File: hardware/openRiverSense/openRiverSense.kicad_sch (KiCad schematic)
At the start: 42 parts, among them J1 Conn_02x04_Odd_Even, J2 Conn_01x08_Pin, J3 Conn_01x02_Pin, U1 MCP6002T-I_SN, U2 MCP6002T-I_SN, U3 MCP6002T-I_SN, U4 AO3401A, U5 MCP6002T-I_SN

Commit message: PCB Design Move to UF2 bootloader Move to Adafruit TinyUSB for mass storage Update Formatting Flip UI orientation Change to PWM Backlight
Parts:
- removed C11, C2, C7, C8: 0402,100nF,16V,X7R, C_0402_1005Metric, symbol jlcpcb-basic-capacitor:0402,100nF,16V,X7R
- removed C5: 0402,10uF,6.3V,X5R, C_0402_1005Metric, symbol jlcpcb-basic-capacitor:0402,10uF,6.3V,X5R
- removed D1: ZMM3V3, footprint:LL-34_L3.5-W1.5-RD, symbol jlcpcb-diodes:ZMM3V3
- removed J1: Conn_02x04_Odd_Even, Connector_PinHeader_2.00mm:PinHeader_2x04_P2.00mm_Horizontal, symbol Connector_Generic:Conn_02x04_Odd_Even
- removed J2: Conn_01x08_Pin, Connector_PinHeader_2.54mm:PinHeader_1x08_P2.54mm_Vertical, symbol Connector:Conn_01x08_Pin
- removed J3: Conn_01x02_Pin, Connector_Wire:SolderWire-0.1sqmm_1x02_P3.6mm_D0.4mm_OD1mm, symbol Connector:Conn_01x02_Pin
- removed JP1: SolderJumper_2_Bridged, Jumper:SolderJumper-2_P1.3mm_Bridged_Pad1.0x1.5mm, symbol Jumper:SolderJumper_2_Bridged
- removed L1, L2, L3: GZ1608D601TF, Inductor_SMD:L_0603_1608Metric, symbol jlcpcb-inductors-ferrite-beads:GZ1608D601TF
- removed LED1: Green, LED_SMD:LED_0603_1608Metric, symbol jlcpcb-diodes:19-217_GHC-YR1S2_3T
- removed R1, R3: 0603,22k, R_0603_1608Metric, symbol jlcpcb-basic-resistor:0603,22k
- removed R10: 0805,16k, R_0805_2012Metric, symbol jlcpcb-basic-resistor:0805,16k
- removed R11, R12: 0402,10k, R_0402_1005Metric, symbol jlcpcb-basic-resistor:0402,10k
- removed R13: 0402,100k, R_0402_1005Metric, symbol jlcpcb-basic-resistor:0402,100k
- removed R15, R7: 0603,20k, R_0603_1608Metric, symbol jlcpcb-basic-resistor:0603,20k
- removed R16, R2, R5: 0603,10k, R_0603_1608Metric, symbol jlcpcb-basic-resistor:0603,10k
- removed R17, R9: 0603,5.1k, R_0603_1608Metric, symbol jlcpcb-basic-resistor:0603,5.1k
- removed R4: 0603,18k, R_0603_1608Metric, symbol jlcpcb-basic-resistor:0603,18k
- removed R6: 0603,11k, R_0603_1608Metric, symbol jlcpcb-basic-resistor:0603,11k
- removed R8: 0603,51k, R_0603_1608Metric, symbol jlcpcb-basic-resistor:0603,51k
- removed U1, U2, U3, U5: MCP6002T-I_SN, footprint:SOIC-8_L4.9-W3.9-P1.27-LS6.0-BL, symbol jlcpcb-analog:MCP6002T-I_SN
- added B1: CR1220, footprint:BAT-SMD_BS-12-B2AA002, symbol jlcpcb-extended:CR1220
- added BMS1: Li-ion 500mA TP4057, footprint:SOT-23-6_L2.9-W1.6-P0.95-LS2.8-BL, symbol jlcpcb-power:Li-ion 500mA TP4057
- added BMS2: SLM6500, footprint:SOP-8_L4.9-W3.9-P1.27-LS6.0-BL-EP, symbol jlcpcb-extended:SLM6500
- added C11, C13, C2, C7: 10uF, footprint:0402_1005Metric, symbol jlcpcb-basic-capacitor:0402,10uF,6.3V,X5R
- added C12, C15: 100nF, footprint:0402_1005Metric, symbol jlcpcb-basic-capacitor:0402,100nF,16V,X7R
- added C14: 0402,1uF,25V,X5R, footprint:0402_1005Metric, symbol jlcpcb-basic-capacitor:0402,1uF,25V,X5R
- added C16: 10uF,6.3V, footprint:0402_1005Metric, symbol jlcpcb-basic-capacitor:0402,10uF,6.3V,X5R
- added C17: 0603,22uF,6.3V,X5R, footprint:0603_1608Metric, symbol jlcpcb-basic-capacitor:0603,22uF,6.3V,X5R
- added C5: 0603,10uF,10V,X5R, footprint:0603_1608Metric, symbol jlcpcb-basic-capacitor:0603,10uF,10V,X5R
- added C8: 0402,10uF,6.3V,X5R, footprint:0402_1005Metric, symbol jlcpcb-basic-capacitor:0402,10uF,6.3V,X5R
- added D1, D2, D3, D5, D6: 1N4148WS_T4, footprint:SOD-323_L1.8-W1.3-LS2.5-RD, symbol jlcpcb-diodes:1N4148WS_T4
- added D4: P6SMB6_8CA-C78395, footprint:SMB_L4.6-W3.6-LS5.3-BI, symbol jlcpcb-diodes:P6SMB6_8CA-C78395
- added ESD1: SRV05, footprint:SOT-23-6_L2.9-W1.6-P0.95-LS2.8-BR, symbol jlcpcb-diodes:SRV05
- added K1: ~, Kea Progmon:mpcie-full-card, symbol Kea Progmon:Kea_Progmon
- added L1: 3.3uH,6A, footprint:IND-SMD_L7.3-W6.8, symbol jlcpcb-extended:3.3uH,6A
- added LDO1, LDO2: XC6220B331MR-G, footprint:SOT-25_L3.0-W1.6-P0.95-LS2.8-TL, symbol jlcpcb-extended:XC6220B331MR-G
- added LED1, LED2, LED5, LED9: 0603,Green, footprint:LED0603, symbol jlcpcb-diodes:0603,Green
- added LED3, LED4, LED6, LED7, LED8: 0603,Yellow, footprint:LED0603, symbol jlcpcb-diodes:0603,Yellow
- added P1: USB-C, footprint:USB-C-SMD_G-SWITCH_GT-USB-7010ASV, symbol jlcpcb-extended:USB C
- added P2, P3: JSTSH_01x06_Vertical, footprint:CONN-SMD_6P-P1.00_DEALON_1.0-6PS, symbol jlcpcb-extended:JSTSH_01x06_Vertical
- added R1, R18, R34, R35: 100k, footprint:0402_1005Metric, symbol jlcpcb-basic-resistor:0402,100k
- added R10, R13, R27, R28, R30, R38, R41, R5, R7, R9: 0402,5.1k, footprint:0402_1005Metric, symbol jlcpcb-basic-resistor:0402,5.1k
- added R11, R21, R29, R36, R8: 0402,100k, footprint:0402_1005Metric, symbol jlcpcb-basic-resistor:0402,100k
- added R15, R16, R22, R6: 0402,10k, footprint:0402_1005Metric, symbol jlcpcb-basic-resistor:0402,10k
- added R19, R25: 0402,330, footprint:0402_1005Metric, symbol jlcpcb-basic-resistor:0402,330
- added R2, R26, R33: 47k, footprint:0402_1005Metric, symbol jlcpcb-basic-resistor:0402,47k
- added R20, R23, R24: 0402,47k, footprint:0402_1005Metric, symbol jlcpcb-basic-resistor:0402,47k
- added R3: 0603,330, footprint:0603_1608Metric, symbol jlcpcb-basic-resistor:0603,330
- added R31, R39: 100m, footprint:1206_3216Metric, symbol jlcpcb-basic-resistor:1206,100m
- added R32, R37: 0402,0,1A, footprint:0402_1005Metric, symbol jlcpcb-basic-resistor:0402,0,1A
- added R4: 0603,100k, footprint:0603_1608Metric, symbol jlcpcb-basic-resistor:0603,100k
- added R40: 0402,150k, footprint:0402_1005Metric, symbol jlcpcb-basic-resistor:0402,150k
- added R42: 0402,33k, footprint:0402_1005Metric, symbol jlcpcb-basic-resistor:0402,33k
- added SW1: Reset, footprint:SW-SMD_4P-L5.1-W5.1-P3.70-LS6.5-TL-2, symbol jlcpcb-switches:TS-1187A-B-A-B
- added SW2: UP_Button, footprint:SW-TH_4P-L12.0-W12.0-P5.00-LS12.5-EH, symbol jlcpcb-extended:Push_Button_SKHCBGA010
- added SW3: ENTER_Button, footprint:SW-TH_4P-L12.0-W12.0-P5.00-LS12.5-EH, symbol jlcpcb-extended:Push_Button_SKHCBGA010
- added SW4: DOWN_Button, footprint:SW-TH_4P-L12.0-W12.0-P5.00-LS12.5-EH, symbol jlcpcb-extended:Push_Button_SKHCBGA010
- added TFT1: ~, IPS Display:IPS Display, symbol IPS Display:IPS_Display
- added TP1: VBACK, footprint:TestPoint_Pad_D1.0mm, symbol Connector:TestPoint
- added TP10: +BATT, footprint:TestPoint_Pad_D1.0mm, symbol Connector:TestPoint
- added TP11, TP2: TestPoint, footprint:TestPoint_Pad_D1.0mm, symbol Connector:TestPoint
- added TP13: NTC, footprint:TestPoint_Pad_D1.0mm, symbol Connector:TestPoint
- added TP3: MON_EN, footprint:TestPoint_Pad_D1.0mm, symbol Connector:TestPoint
- added TP4: CHRG, footprint:TestPoint_Pad_D1.0mm, symbol Connector:TestPoint
- added TP5: STDBY, footprint:TestPoint_Pad_D1.0mm, symbol Connector:TestPoint
- added TP6: CS, footprint:TestPoint_Pad_D1.0mm, symbol Connector:TestPoint
- added TP7: VCC, footprint:TestPoint_Pad_D1.0mm, symbol Connector:TestPoint
- added TP9: VUSB, footprint:TestPoint_Pad_D1.0mm, symbol Connector:TestPoint
- added U1, U6: AO3400A, footprint:SOT-23-3_L2.9-W1.6-P1.90-LS2.8-BR, symbol jlcpcb-transistors:AO3400A
- added U2, U7: AO3401A, footprint:SOT-23_L2.9-W1.3-P1.90-LS2.4-BR, symbol jlcpcb-transistors:AO3401A
- added U3: ATGM332D-5N31, footprint:GSM-SMD_ATGM332D-5N31, symbol jlcpcb-extended:ATGM332D-5N31
- added U5: ESP32-S2-SOLO-N4R2, footprint:WIRELM-SMD_ESP32-S3-WROOM-1, symbol jlcpcb-extended:ESP32-S2-SOLO-N4R2
- added U8: GPS_Antenna_25x25mm, footprint:ANT-TH_KH-GPS252504-WY, symbol jlcpcb-extended:GPS_Antenna_25x25mm
- C1, C10, C3, C4, C6, C9: value 0402,100nF,16V,X7R -> 100nF; footprint C_0402_1005Metric -> footprint:0402_1005Metric
- R14: footprint R_0402_1005Metric -> footprint:0402_1005Metric
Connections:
- net NITRATE_OUT is gone; now on net GND: C6.1
- net ORP_OUT is gone; now on net VBAT_MON: C9.1
- net GND: now also C10.2, B1.2 (-), BMS1.2 (GND), BMS2.1 (GND), BMS2.9 (EP), C11.2, C12.2, C13.2, C14.2, C15.2, C16.2, C17.2, C2.2, C5.2, C7.2, C8.2, D4.2, ESD1.2 (GND), K1.1 (GND), K1.15 (GND), K1.16 (GND), K1.17 (GND), K1.18 (GND), K1.2 (GND), K1.51 (GND), K1.52 (GND), LDO1.2 (VSS), LDO2.2 (VSS), P1.2 (GND), P2.2, P2.7, P2.8, P3.5, P3.6, P3.7, P3.8, R1.2, R11.2, R13.2, R15.1, R18.2, R21.2, R30.2, R34.2, R35.2, R36.2, R38.2, R4.2, R40.2, R5.2, R8.2, SW1.3 (C), SW1.4 (D), TFT1.1 (GND), U1.2 (S), U3.10 (GND), U3.12 (GND), U3.13 (GND), U3.24 (GND), U5.1 (GND), U5.40 (GND), U5.41 (EPAD), U6.2 (S); no longer C6.2
- net +3V3_S3: now reaches U4.3 (D)
- net +3V3_S3: now also K1.29 (3V3_S3); no longer C10.2
- net +3.3V renamed +3V3
- net +3V3: now also C6.2, C7.1, D2.2 (A), K1.19 (3V3_S1), LDO2.5 (VOUT), LED2.2 (A), LED6.2 (A), LED7.2 (A), R22.2, R3.1, R6.1, SW2.1, SW3.1, SW4.1, TP2.1, U5.2 (3V3); no longer C1.1
- net EC_EN renamed VBAT_MON
- net VBAT_MON: now also R15.2, U5.5 (IO5)
- net EC_OUT renamed +3V3_OUT
- net +3V3_OUT: now also C2.1, K1.21 (3V3_S2), LDO1.5 (VOUT), LED1.2 (A), LED3.2 (A), LED4.2 (A), P2.1, R20.1, R23.1, R24.1, TFT1.4 (VDD), TP11.1, U3.23 (VCC)
- net TEMP_INA: no longer names the net of C4.1
- net TEMP_INA: now also D2.1 (K), D3.1 (K), TP1.1, U3.22 (VBAT)
- new net: LED7.1 (C), R27.1
- new net: LED2.1 (C), R7.1
- new net: LED5.1 (C), R13.1
- new net: B1.1 (+), D1.1 (K), D3.2 (A)
- new net: R14.2, U2.3 (D)
- new net: BMS1.1 (CHRG), TP4.1
- new net: P1.CC1, R38.1
- new net: P1.CC2, R30.1
- new net: LED3.1 (C), R9.1
- new net: BMS1.5 (STDBY), TP5.1
- new net: BMS1.6 (PROG), R4.1
- new net: LED1.1 (C), R5.1
- new net: D1.2 (A), R3.2
- new net: R19.2, R6.2, U4.1 (G)
- new net: K1.7 (Sense_1A), K1.9 (Sense_1B)
- new net: R1.1, R2.2, SW2.4
- new net: TFT1.2 (LEDK), U6.3 (D)
- new net: BMS2.3 (Charging), LED8.1 (C)
- new net: LED8.2 (A), LED9.2 (A), R41.2
- new net: R16.2, TP3.1, U1.3 (D), U2.1 (G)
- new net: R33.2, R34.1, SW4.4
- new net: R26.2, R35.1, SW3.4
- new net: LED4.1 (C), R10.1
- new net: R21.1, R25.2, U6.1 (G)
- new net: LED6.1 (C), R28.1
- new net: BMS2.4 (Charged), LED9.1 (C)
- new net +3V3_OUT_EN: LDO1.3 (CE), R18.1, U5.31 (IO38)
- new net +3V3_S3_EN: R19.1, U5.6 (IO6)
- new net +BATT: BMS1.3 (BAT), C8.1, K1.23 (5VS1), R16.1, R32.1, TFT1.3 (LEDA), U2.2 (S), U7.3 (D)
- new net +BATT_2A: BMS2.6 (BAT+), C17.1, P3.1, P3.2, R31.2, R32.2, R39.2, TP10.1
- new net +Solar: BMS1.4 (VCC), C5.1, P3.4
- new net 100kNTC: BMS2.5 (TS_Temp), P3.3, R40.1, R42.2, TP13.1
- new net D+: ESD1.1 (IO1), P1.DP (D+), U5.14 (IO20)
- new net D-: ESD1.3 (IO2), P1.DN (D-), U5.13 (IO19)
- new net DOWN: C15.1, R33.1, U5.18 (IO10)
- new net EN: C14.1, K1.4 (EN), R22.1, SW1.1 (A), SW1.2 (B), U5.3 (EN)
- new net ENTER: C12.1, R26.1, U5.20 (IO12)
- new net GPS_PPS: K1.24 (GPS_PPS), LED5.2 (A), U3.3 (1PPS), U5.9 (IO16)
- new net GPS_RX: K1.20 (GPS_RX), R10.2, U3.21 (RXD1), U5.11 (IO18)
- new net GPS_TX: K1.22 (GPS_TX), R9.2, U3.20 (TXD1), U5.10 (IO17)
- new net I2C_INT: K1.14 (I2C1INT), P2.5, U5.15 (IO3)
- new net IO0: K1.34 (IO0), U5.27 (IO0)
- new net IO2: K1.38 (IO2), R7.2, U5.38 (IO2)
- new net LCD_BKL: R25.1, U5.21 (IO13)
- new net LCD_CS: R20.2, TFT1.8 (CS), TP6.1, U5.23 (IO21)
- new net LCD_DC: TFT1.7 (D/C), U5.22 (IO14)
- new net LCD_MOSI: R24.2, TFT1.10 (MOSI), U5.28 (IO35)
- new net LCD_RST: TFT1.11 (RST), U5.24 (IO33)
- new net LCD_SCK: R23.2, TFT1.9 (SCK), U5.29 (IO36)
- new net LX: BMS2.8 (LX_Switching), L1.1
- new net RX: K1.10 (RX), R28.2, U5.36 (RXD0)
- new net SCL: K1.6 (SCL1), P2.4, U5.17 (IO9)
- new net SDA: K1.12 (SDA1), P2.3, U5.12 (IO8)
- new net TCK: K1.42 (TCK), U5.32 (IO39)
- new net TDI: K1.46 (TDI), U5.34 (IO41)
- new net TDO: K1.40 (TDO), U5.33 (IO40)
- new net TEMP_OW: P2.6, U5.8 (IO15)
- new net TMS: K1.44 (TMS), U5.35 (IO42)
- new net TX: K1.8 (TX), R27.2, U5.37 (TXD0)
- new net UP: C1.1, R2.1, U5.19 (IO11)
- new net VBAT_MON_EN: R8.1, U1.1 (G), U5.4 (IO4)
- new net VBUS: D5.2 (A), D6.2 (A), ESD1.5 (VCC), R29.1, R36.1, R37.1, R41.1, R42.1, U7.1 (G)
- new net VBUS_2A: BMS2.2 (VCC), C16.1, D4.1, K1.11 (5V), K1.13 (5V), P1.3 (VBUS), R37.2, TP9.1
- new net VCC: C11.1, C13.1, D5.1 (K), D6.1 (K), K1.25 (5VS2), LDO1.1 (VIN), LDO2.1 (VIN), LDO2.3 (CE), TP7.1, U7.2 (S)
- new net VS: BMS2.7 (VS_Sense), L1.2, R31.1, R39.1
- new net VUSB_MON: C10.1, R11.1, R29.2, U5.39 (IO1)
- new net antenna: U3.11 (RF_IN), U8.1 (ANT)
- no-connect marks 3 -> 43
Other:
- note added: "100k = 10mA 47k = 21mA 20k = 50mA"
- note removed: "1.6k-66"
- note removed: "455mV-22mV"
- note removed: "Non-Inverting op-amp Gain 3.2"
- note removed: "Non-Inverting op-amp Gain 4.9"
- note removed: "Ofset by 0.100V"
- note removed: "Ofset by 1.251V"

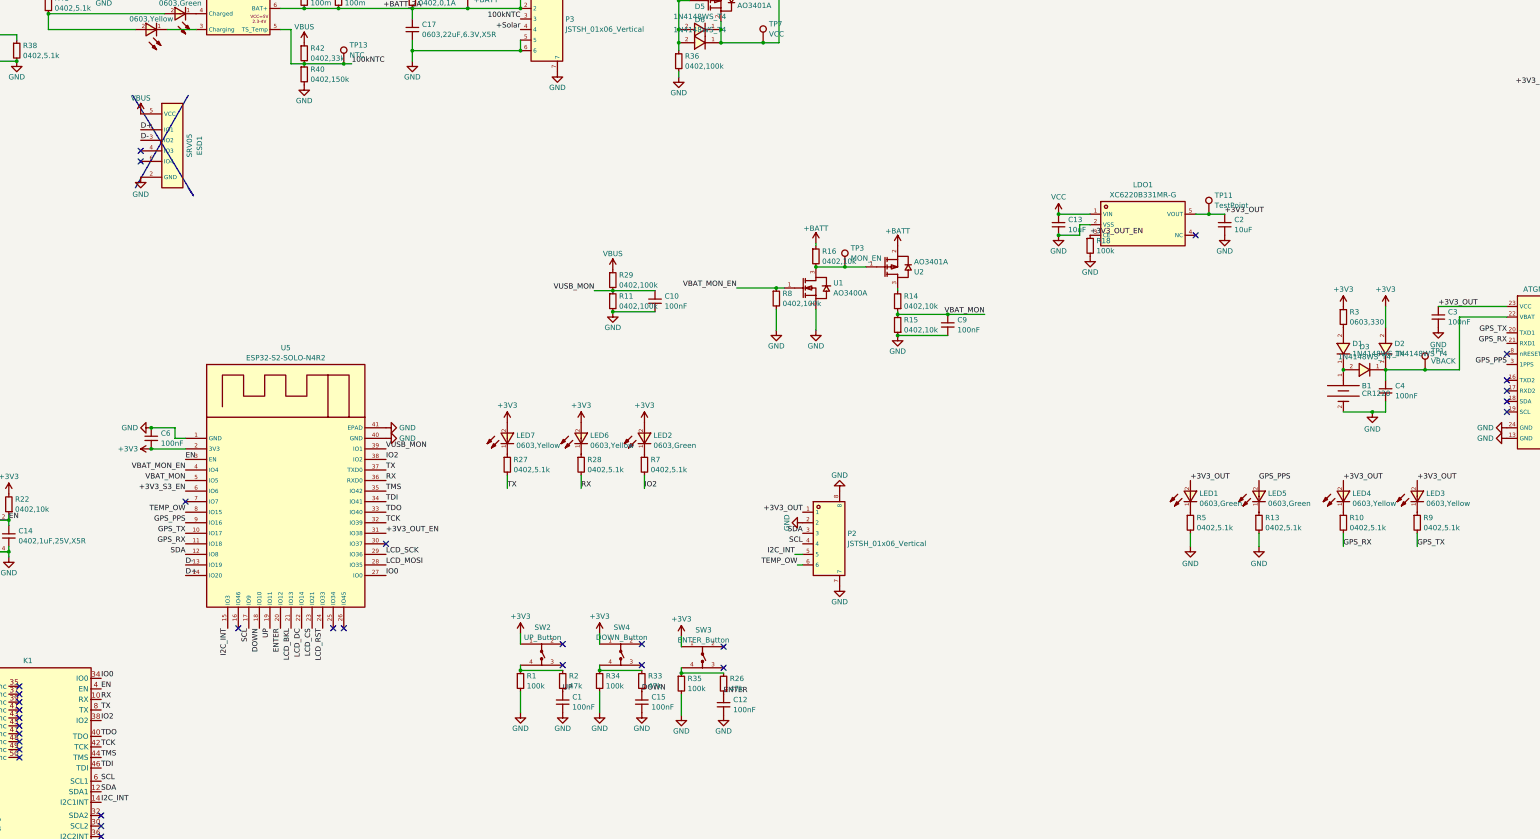
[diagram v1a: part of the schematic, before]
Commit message: - setup state machine - add adafruit.io - fix battery soc calculation - increase gps baud rate
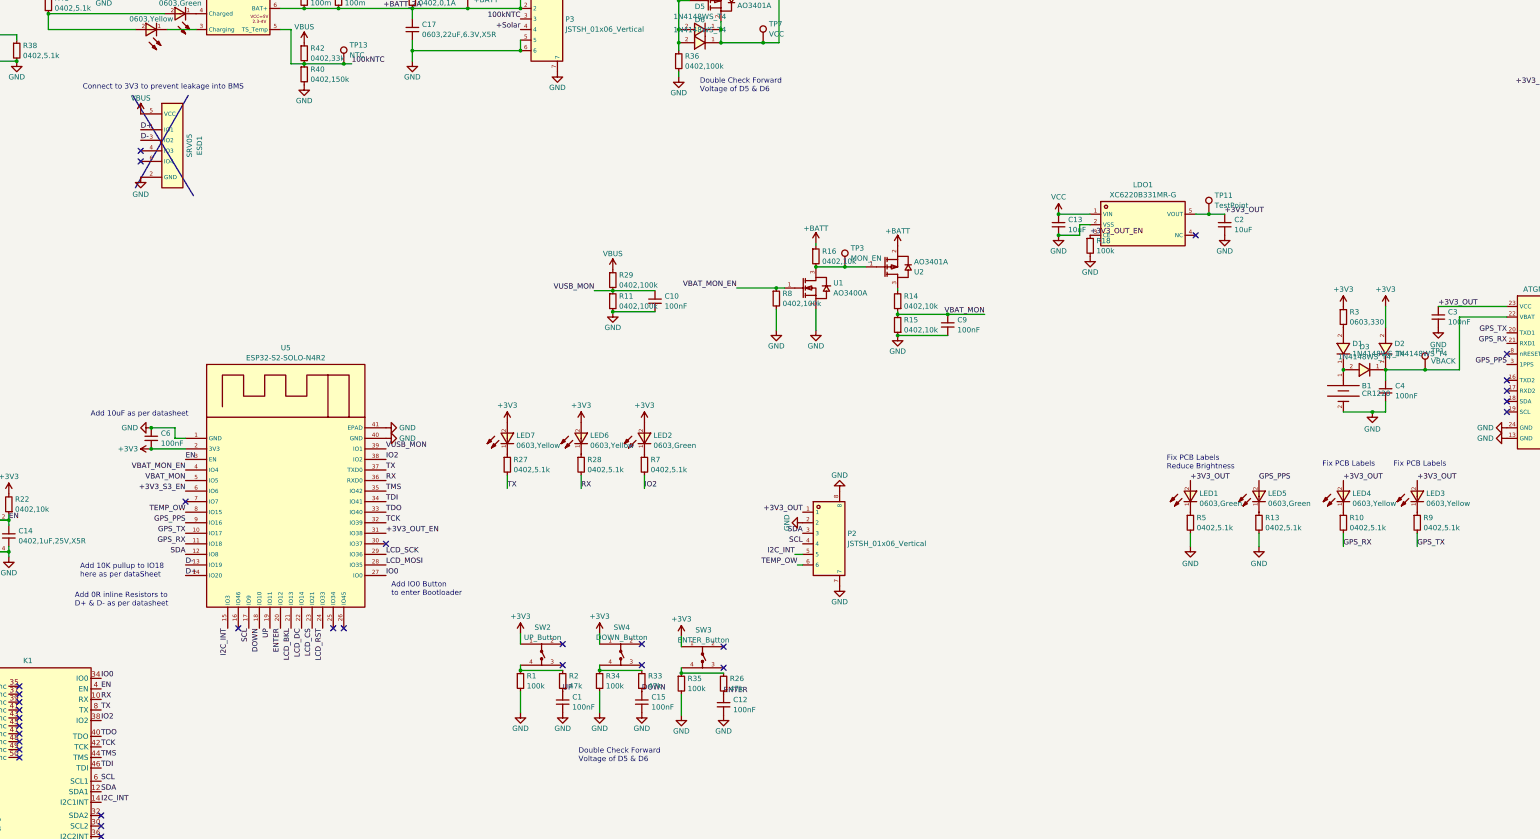
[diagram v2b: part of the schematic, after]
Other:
- note added: "Add 0R inline Resistors to D+ & D- as per datasheet"
- note added: "Add 10K pullup to IO18 here as per dataSheet"
- note added: "Add 10uF as per datasheet"
- note added: "Add IO0 Button to enter Bootloader"
- note added: "Connect to 3V3 to prevent leakage into BMS"
- note added: "Double Check Forward Voltage of D5 & D6"
- note added: "Fix PCB Labels"
- note added: "Fix PCB Labels Reduce Brightness"
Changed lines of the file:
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@@
-    (stroke (width 0) (type default))
-  )
-  (polyline (pts (xy 97.79 285.75) (xy 96.52 283.845))
     (stroke (width 0) (type default))
   )
@@
     (stroke (width 0) (type default))
   )
+  (text "Add 10K pullup to IO18 \nhere as per dataSheet" (at 70.485 377.825 0)
+    (effects (font (size 1.27 1.27)) (justify left bottom))
+  )
+  (text "Double Check Forward \nVoltage of D5 & D6" (at 190.5 422.275 0)
+    (effects (font (size 1.27 1.27)) (justify left bottom))
+  )
+  (text "Add 10uF as per datasheet" (at 73.025 339.09 0)
+    (effects (font (size 1.27 1.27)) (justify left bottom))
+  )
+  (text "Fix PCB Labels\nReduce Brightness" (at 332.105 351.79 0)
+    (effects (font (size 1.27 1.27)) (justify left bottom))
+  )
+  (text "Fix PCB Labels" (at 369.57 351.155 0)
+    (effects (font (size 1.27 1.27)) (justify left bottom))
+  )
+  (text "Fix PCB Labels" (at 386.715 351.155 0)
+    (effects (font (size 1.27 1.27)) (justify left bottom))
+  )
+  (text "Add 0R inline Resistors to \nD+ & D- as per datasheet"
+    (at 69.215 384.81 0)
+    (effects (font (size 1.27 1.27)) (justify left bottom))
+  )
+  (text "Add IO0 Button\nto enter Bootloader" (at 145.415 382.27 0)
+    (effects (font (size 1.27 1.27)) (justify left bottom))
+  )
+  (text "Double Check Forward \nVoltage of D5 & D6" (at 219.71 260.985 0)
+    (effects (font (size 1.27 1.27)) (justify left bottom))
+  )
+  (text "Connect to 3V3 to prevent leakage into BMS" (at 71.12 260.35 0)
+    (effects (font (size 1.27 1.27)) (justify left bottom))
+  )
   (text "100k = 10mA\n47k = 21mA\n20k = 50mA" (at 328.93 148.59 0)

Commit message: basic sensor setup
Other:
- note added: "Ferrite Bead?"
- note added: "More Decoupling Caps in the pF range?"
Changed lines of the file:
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@@
+    (effects (font (size 1.27 1.27)) (justify left bottom))
+  )
+  (text "More Decoupling Caps in the pF range?" (at 387.985 300.99 0)
     (effects (font (size 1.27 1.27)) (justify left bottom))
   )
@@
     (effects (font (size 1.27 1.27)) (justify left bottom))
   )
+  (text "Ferrite Bead?" (at 387.985 298.45 0)
+    (effects (font (size 1.27 1.27)) (justify left bottom))
+  )

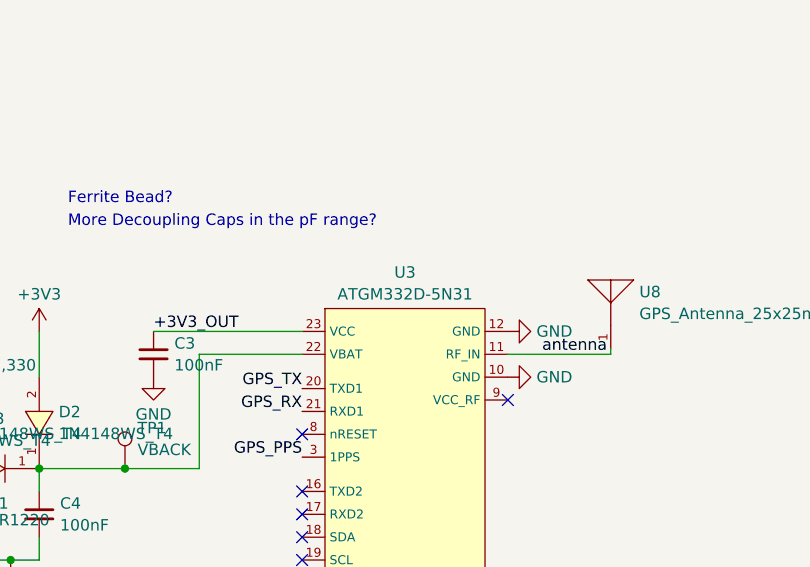
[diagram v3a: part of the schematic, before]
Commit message: -added CAD models -moved to KiCAD 8.0 -clang formatting -rebuild sensor calibration -add logging and analytics file -added adaptive backlight -added work hours for gps sync
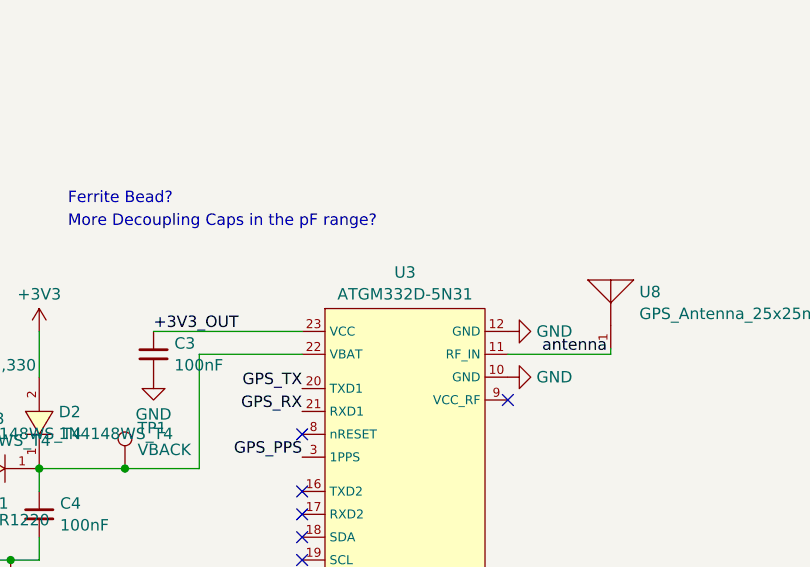
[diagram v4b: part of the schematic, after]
